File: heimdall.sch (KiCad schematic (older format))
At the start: 14 parts, among them P1 CONN, U1 ESP-01, U2 TLP222A, U3 TPS62177

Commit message: Minor shuffling and finishing up.
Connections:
- net GND: now also U3.4 (NC)
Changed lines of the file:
@@
 L GND #PWR014
 U 1 1 575784AE
-P 2150 2400
-F 0 "#PWR014" H 2150 2150 50  0001 C CNN
-F 1 "GND" H 2150 2250 50  0000 C CNN
-F 2 "" H 2150 2400 50  0000 C CNN
-F 3 "" H 2150 2400 50  0000 C CNN
-	1    2150 2400
+P 2150 2500
+F 0 "#PWR014" H 2150 2250 50  0001 C CNN
+F 1 "GND" H 2150 2350 50  0000 C CNN
+F 2 "" H 2150 2500 50  0000 C CNN
+F 3 "" H 2150 2500 50  0000 C CNN
+	1    2150 2500
 	1    0    0    -1
 $EndComp
@@
 	2050 2300 2150 2300
 Wire Wire Line
-	2150 2200 2150 2400
+	2150 2200 2150 2500
 Connection ~ 2250 2000
 Wire Wire Line
@@
 	5300 1400 5350 1400
 Connection ~ 5350 1400
+Wire Wire Line
+	2150 2400 2050 2400
+Connection ~ 2150 2400
 $EndSCHEMATC

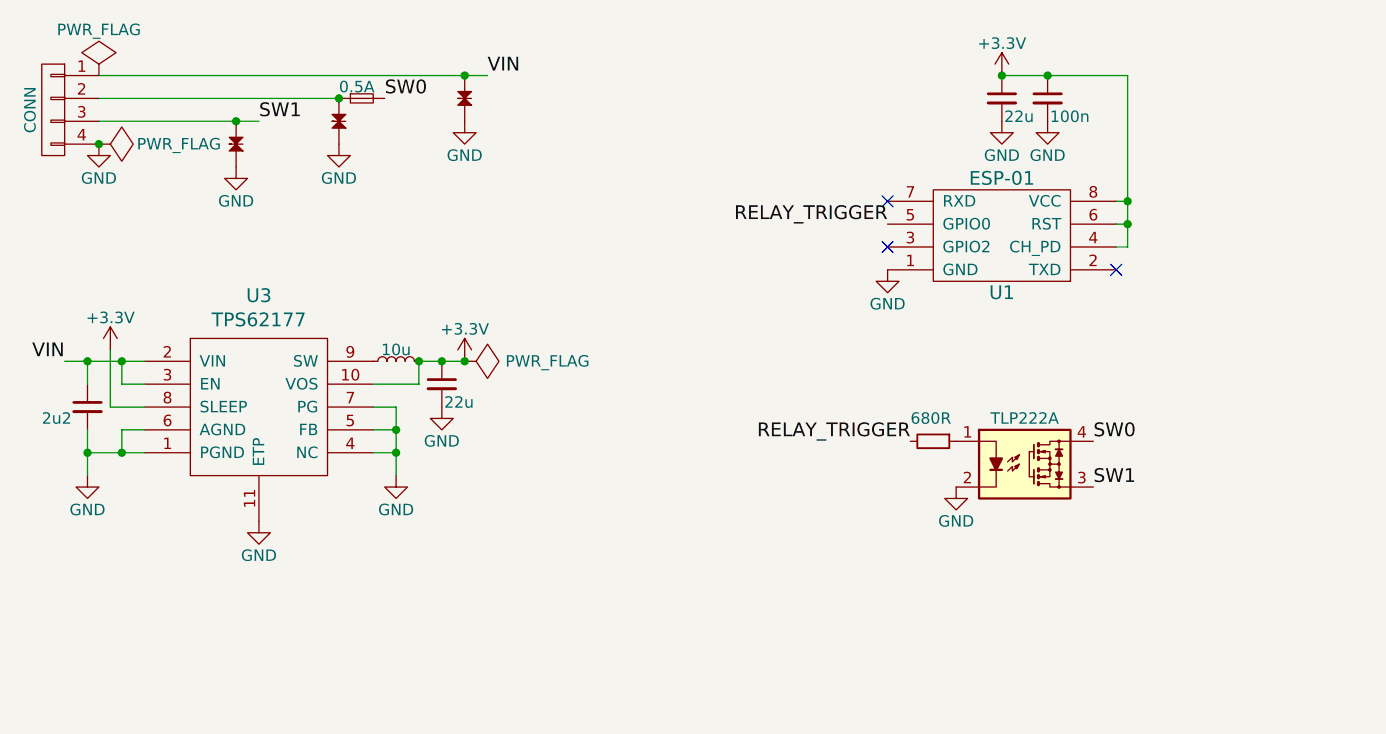
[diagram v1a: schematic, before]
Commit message: Various shuffling
* Switched to agg footprints where possible
* Farnell numbers and data sheets
* Status LEDs for dev
* Schematic shuffling
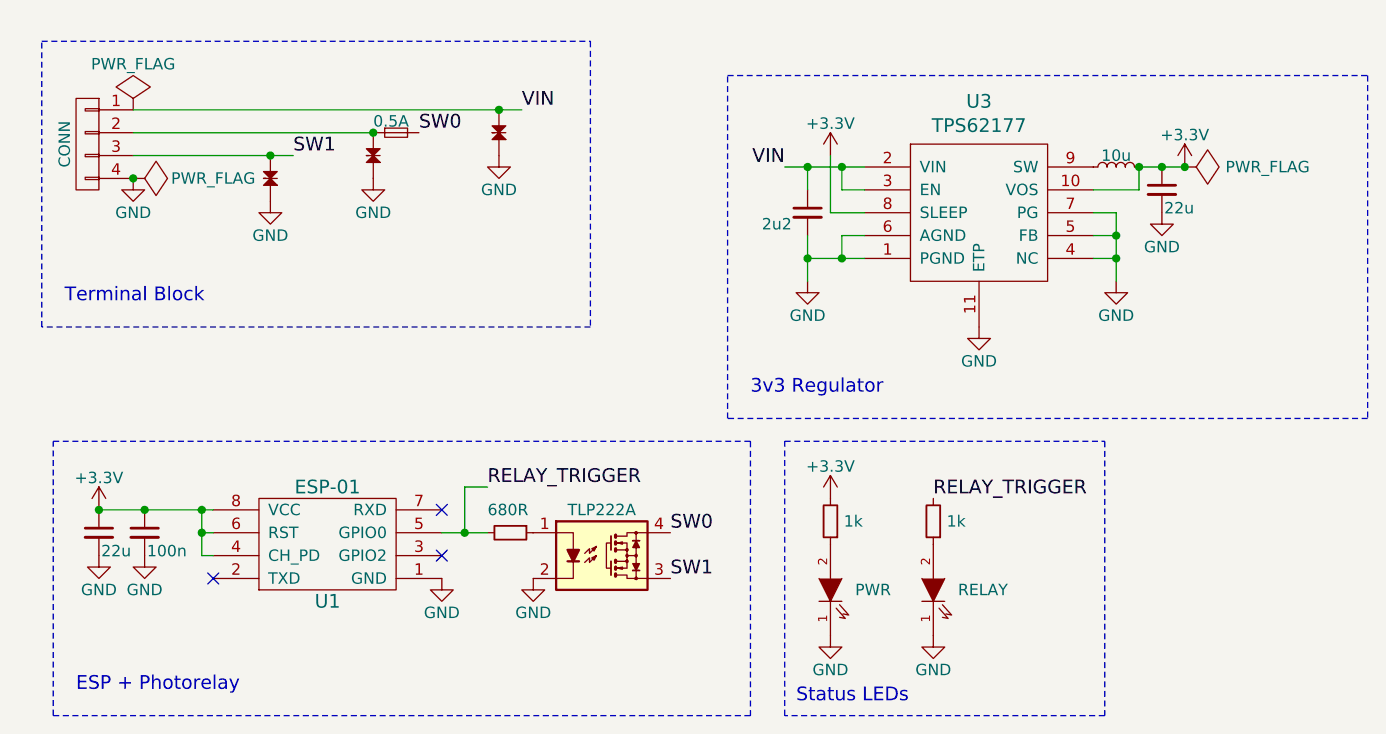
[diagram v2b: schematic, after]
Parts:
- added D2: PWR, agg:0603-LED, symbol LED
- added D5: RELAY, agg:0603-LED, symbol LED
- added R2, R3: 1k, agg:0603, symbol R_Small
- C1: footprint Capacitors_SMD:C_0603 -> agg:0603; Farnell 2496833 -> 2494232
- C4: footprint Capacitors_SMD:C_0603 -> agg:0603; Farnell 2496833 -> 2524817
- C5: footprint Capacitors_SMD:C_0603 -> agg:0603; Farnell 2497155 -> 2494232
- C6: footprint Capacitors_SMD:C_0603 -> agg:0603; Farnell 2496833 -> 1845734
- D1: footprint Resistors_SMD:R_0603 -> agg:0603
- F1: footprint Resistors_SMD:R_1206 -> agg:1206; Farnell 9921834 -> 1843802
- L1: Farnell (none) -> 1869745
- R1: footprint Resistors_SMD:R_0603 -> agg:0603; Farnell (none) -> 9331441
- U1: Farnell (none) -> 1593489
- U2: footprint Housings_DIP:DIP-4_W7.62mm -> Housings_DIP:DIP-4_W7.62mm_LongPads; Farnell (none) -> 1761595
- U3: Farnell (none) -> 2255014
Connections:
- net +3V3: now also R2.2
- net GND: now also D2.1 (K), D5.1 (K)
- net RELAY_TRIGGER: now also R3.2
- new net: D2.2 (A), R2.1
- new net: D5.2 (A), R3.1
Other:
- note added: "3v3 Regulator"
- note added: "ESP + Photorelay"
- note added: "Status LEDs"
- note added: "Terminal Block\n"
- moved on the sheet: U1, U3

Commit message: Various
* changed TVS diodes over to new agg:SMA
* Swapped terminal block for one from HL
* Setup for board panelizing
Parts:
- D3, D4: footprint Diodes_SMD:SMA_Standard -> agg:DO-214AC-SMA
- P1: footprint footprints:CTB1500-4 -> footprints:MKDS-4; Farnell CN11535 -> 2314975
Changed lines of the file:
@@
 F 0 "P1" H 800 1300 50  0001 C CNN
 F 1 "CONN" V 900 1050 50  0000 C CNN
-F 2 "footprints:CTB1500-4" H 800 1050 50  0001 C CNN
-F 3 "" H 800 1050 50  0000 C CNN
-F 4 "CN11535" H 800 1050 60  0001 C CNN "Farnell"
+F 2 "footprints:MKDS-4" H 800 1050 50  0001 C CNN
+F 3 "http://www.farnell.com/datasheets/1702031.pdf" H 800 1050 50  0001 C CNN
+F 4 "2314975" H 800 1050 60  0001 C CNN "Farnell"
 	1    800  1050
 	-1   0    0    -1
@@
 F 0 "D3" H 2000 1170 50  0001 L CNN
 F 1 "TVS_Small" V 2050 1150 50  0001 L CNN
-F 2 "Diodes_SMD:SMA_Standard" V 2050 1200 50  0001 C CNN
+F 2 "agg:DO-214AC-SMA" V 2050 1200 50  0001 C CNN
 F 3 "http://www.farnell.com/datasheets/1724007.pdf" V 2050 1100 50  0001 C CNN
 F 4 "1749308" H 2050 1100 60  0001 C CNN "Farnell"
@@
 F 0 "D4" H 1550 1270 50  0001 L CNN
 F 1 "TVS_Small" V 1600 1250 50  0001 L CNN
-F 2 "Diodes_SMD:SMA_Standard" V 1600 1300 50  0001 C CNN
+F 2 "agg:DO-214AC-SMA" V 1600 1300 50  0001 C CNN
 F 3 "http://www.farnell.com/datasheets/1724007.pdf" V 1600 1200 50  0001 C CNN
 F 4 "1749308" H 1600 1200 60  0001 C CNN "Farnell"
@@
 $EndComp
 $Comp
-L GND #PWR020
+L GND #PWR019
 U 1 1 576FD9F6
 P 4500 3200
-F 0 "#PWR020" H 4500 2950 50  0001 C CNN
+F 0 "#PWR019" H 4500 2950 50  0001 C CNN
 F 1 "GND" H 4500 3050 50  0000 C CNN
 F 2 "" H 4500 3200 50  0000 C CNN
@@
 RELAY_TRIGGER
 $Comp
-L GND #PWR021
+L GND #PWR020
 U 1 1 576FDA71
 P 4050 3200
-F 0 "#PWR021" H 4050 2950 50  0001 C CNN
+F 0 "#PWR020" H 4050 2950 50  0001 C CNN
 F 1 "GND" H 4050 3050 50  0000 C CNN
 F 2 "" H 4050 3200 50  0000 C CNN
@@
 	3850 3550 3850 2350
 $Comp
-L +3.3V #PWR?
+L +3.3V #PWR021
 U 1 1 576FE543
 P 4050 2600
-F 0 "#PWR?" H 4050 2450 50  0001 C CNN
+F 0 "#PWR021" H 4050 2450 50  0001 C CNN
 F 1 "+3.3V" H 4050 2740 50  0000 C CNN
 F 2 "" H 4050 2600 50  0000 C CNN
